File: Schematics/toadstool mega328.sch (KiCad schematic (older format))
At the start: 26 parts, among them CON1 BARREL_JACK, IC1 ATMEGA328P-P, K1 CAP_CONN_LHS, K2 CAP_CONN_RHS, K3 V-SELECT, K4 ICSP, K5 PIN 2-8, K6 PIN 21-28, K7 XTAL, K8 PIN 15-19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

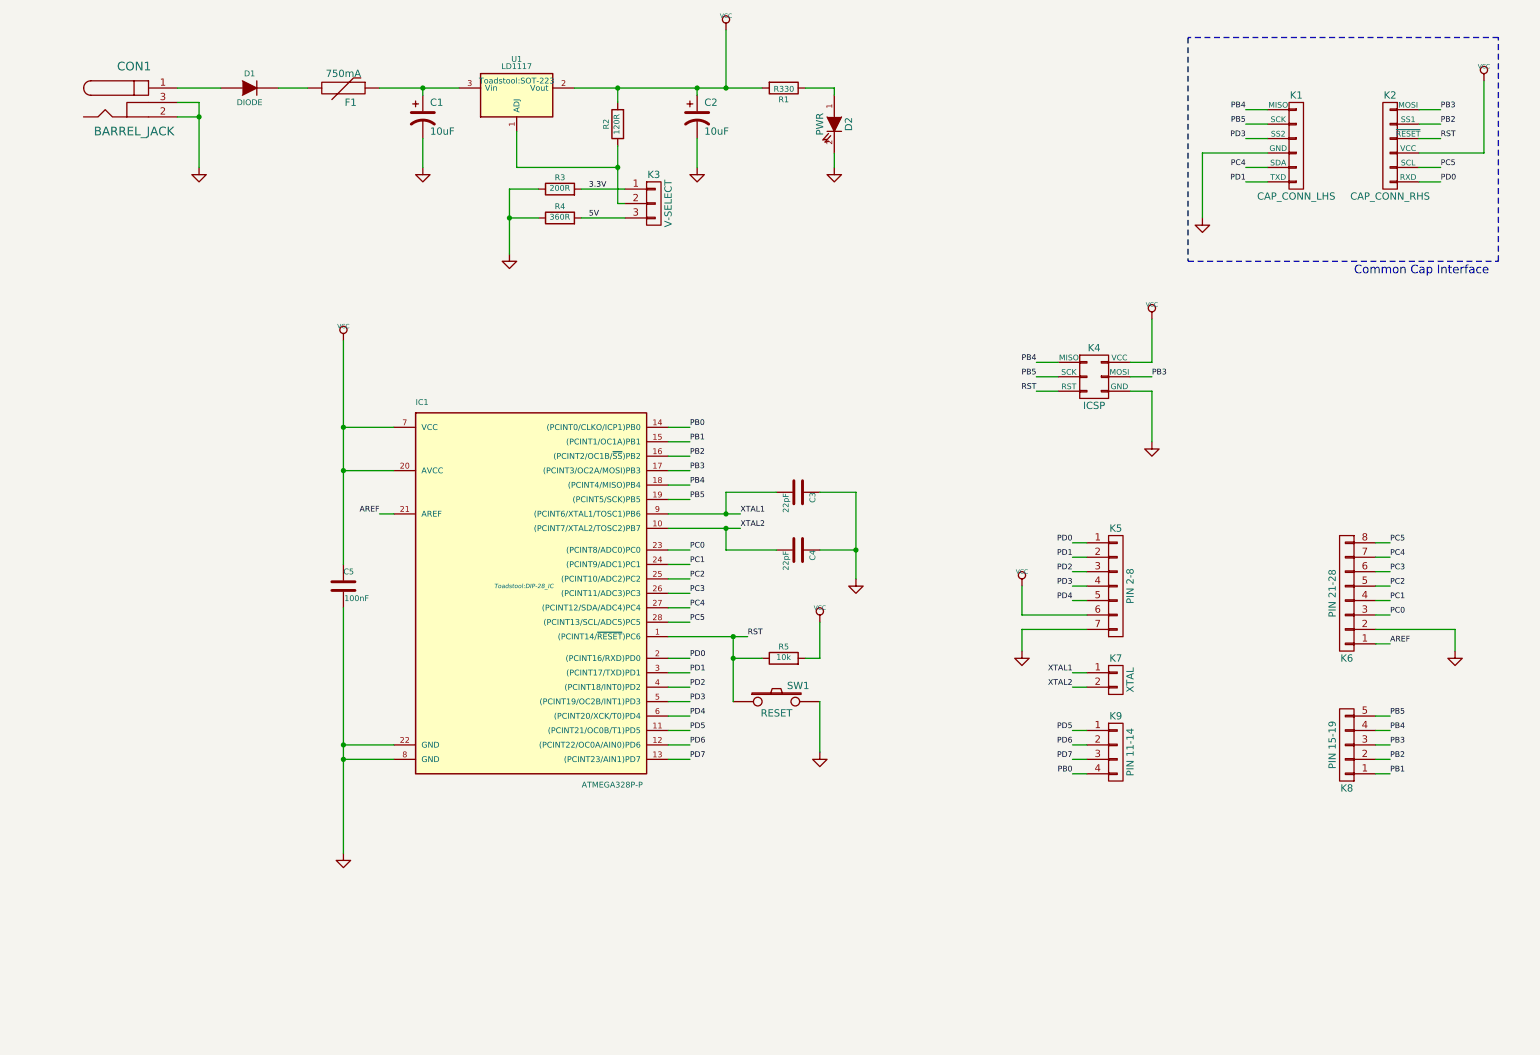
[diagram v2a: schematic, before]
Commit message: Cosmetic Changes to Silkscreen
Cosmetic Changes to Silkscreen
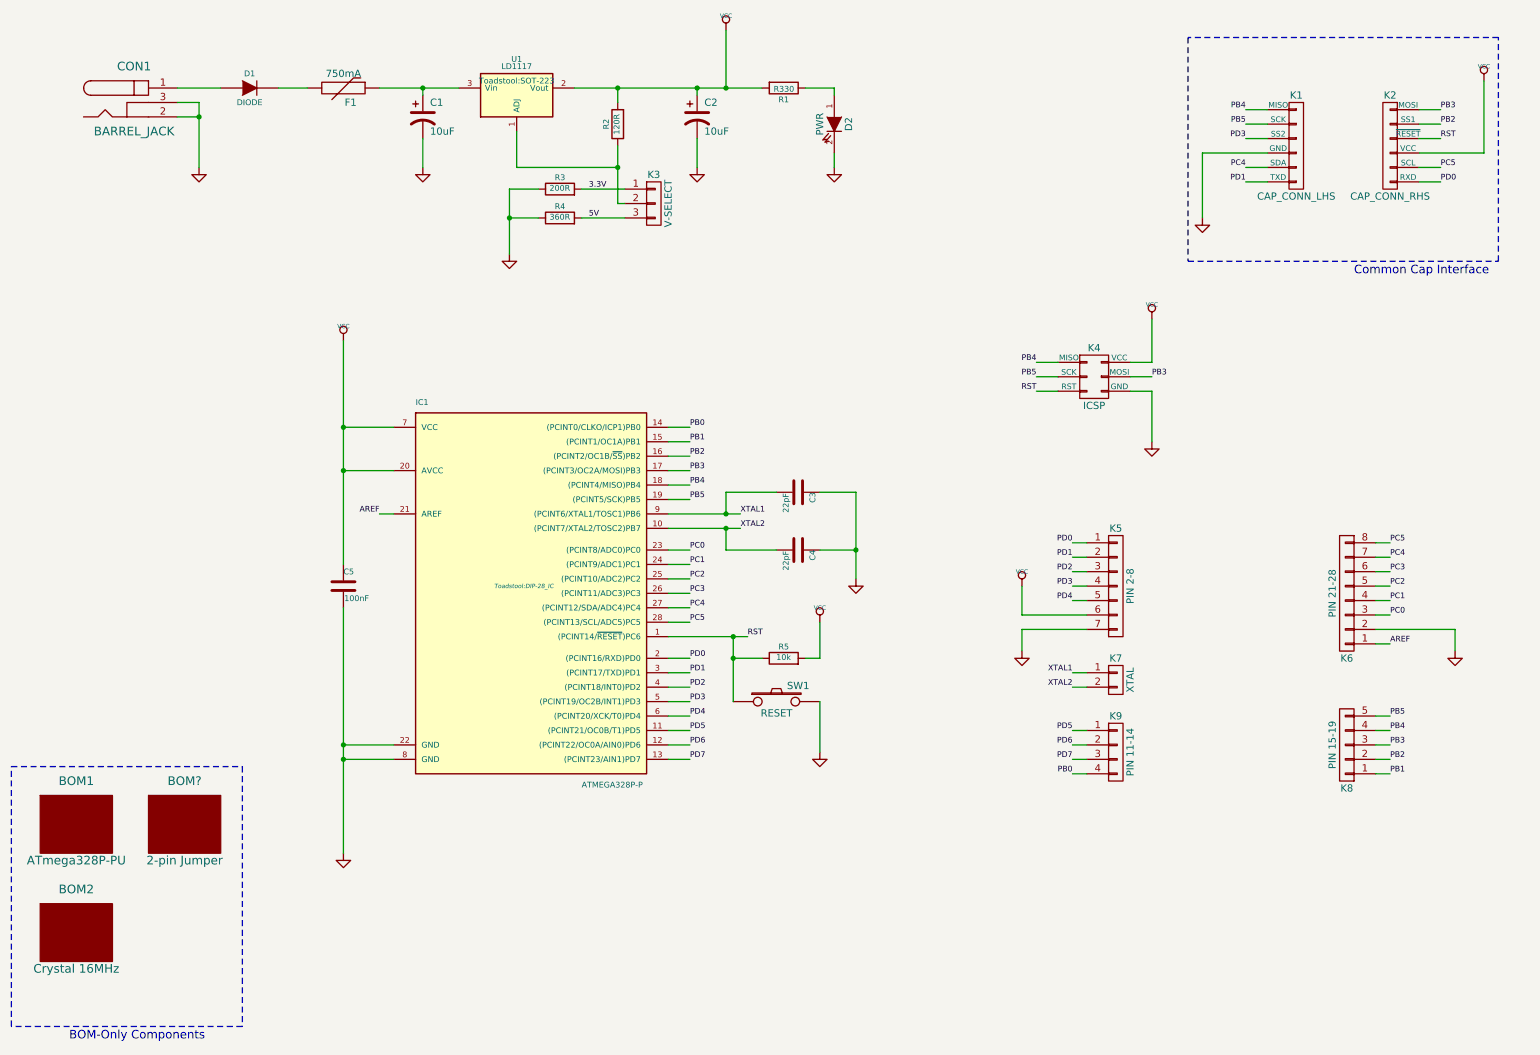
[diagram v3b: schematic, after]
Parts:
- added BOM1: ATmega328P-PU, symbol BOM
- added BOM2: Crystal 16MHz, symbol BOM
- added BOM?: 2-pin Jumper, symbol BOM
- C1, C2: Alt_Manufacturer (none) -> -; Alt_Mfg_Package_Suffix (none) -> -; Alt_Mfg_Part_No (none) -> -; Contract_Manuf_SKU (none) -> 302030059; Manufacturer (none) -> Nichicon; Mfg_Package_Suffix (none) -> -; Mfg_Part_No (none) -> UWX1C100MCL1GB
- C3, C4: Alt_Manufacturer (none) -> -; Alt_Mfg_Package_Suffix (none) -> -; Alt_Mfg_Part_No (none) -> -; Contract_Manuf_SKU (none) -> 0100620P1; Manufacturer (none) -> Kemet; Mfg_Package_Suffix (none) -> -; Mfg_Part_No (none) -> C0805C220J1GACTU
- C5: Alt_Manufacturer (none) -> -; Alt_Mfg_Package_Suffix (none) -> -; Alt_Mfg_Part_No (none) -> -; Contract_Manuf_SKU (none) -> 302010165; Manufacturer (none) -> Kemet; Mfg_Package_Suffix (none) -> -; Mfg_Part_No (none) -> C0805C104K5RACTU
- CON1: Alt_Manufacturer (none) -> Kobiconn; Alt_Mfg_Package_Suffix (none) -> -; Alt_Mfg_Part_No (none) -> 163-5010-E; Contract_Manuf_SKU (none) -> 3410020P1; Manufacturer (none) -> CUI Inc; Mfg_Package_Suffix (none) -> -; Mfg_Part_No (none) -> PJ-002A
- D1: Alt_Manufacturer (none) -> Diodes Inc; Alt_Mfg_Package_Suffix (none) -> -; Alt_Mfg_Part_No (none) -> 1N5817-T; Contract_Manuf_SKU (none) -> 0300070P1; Manufacturer (none) -> STMicroelectronics; Mfg_Package_Suffix (none) -> -; Mfg_Part_No (none) -> 1N5819
- D2: Alt_Manufacturer (none) -> Osram; Alt_Mfg_Package_Suffix (none) -> -; Alt_Mfg_Part_No (none) -> LH R974-LP-1; Contract_Manuf_SKU (none) -> 0330020P1; Manufacturer (none) -> Osram; Mfg_Package_Suffix (none) -> -; Mfg_Part_No (none) -> LH R974
- F1: Alt_Manufacturer (none) -> -; Alt_Mfg_Package_Suffix (none) -> -; Alt_Mfg_Part_No (none) -> -; Contract_Manuf_SKU (none) -> 307010010; Manufacturer (none) -> TE Connectivity; Mfg_Package_Suffix (none) -> -; Mfg_Part_No (none) -> MICROSMD050F-2
- IC1: Alt_Manufacturer (none) -> 3M; Alt_Mfg_Package_Suffix (none) -> -; Alt_Mfg_Part_No (none) -> 4828-3004-CP; Contract_Manuf_SKU (none) -> -; Manufacturer (none) -> Assmann; Mfg_Package_Suffix (none) -> -; Mfg_Part_No (none) -> A 28-LC/7-T
- K1, K2: Alt_Manufacturer (none) -> 4UConnector; Alt_Mfg_Package_Suffix (none) -> -; Alt_Mfg_Part_No (none) -> 15170; Contract_Manuf_SKU (none) -> -; Manufacturer (none) -> Samtec; Mfg_Package_Suffix (none) -> -; Mfg_Part_No (none) -> ESQ-106-12-G-S
- K3: Alt_Manufacturer (none) -> -; Alt_Mfg_Package_Suffix (none) -> -; Alt_Mfg_Part_No (none) -> -; Contract_Manuf_SKU (none) -> 3460810P1; Manufacturer (none) -> Harwin; Mfg_Package_Suffix (none) -> -; Mfg_Part_No (none) -> M20-9990345
- K4: Alt_Manufacturer (none) -> -; Alt_Mfg_Package_Suffix (none) -> -; Alt_Mfg_Part_No (none) -> -; Contract_Manuf_SKU (none) -> 3460180P1; Manufacturer (none) -> 3M; Mfg_Package_Suffix (none) -> -; Mfg_Part_No (none) -> 30306-6002HB
- K5: Alt_Manufacturer (none) -> -; Alt_Mfg_Package_Suffix (none) -> -; Alt_Mfg_Part_No (none) -> -; Contract_Manuf_SKU (none) -> -; Manufacturer (none) -> Wurth; Mfg_Package_Suffix (none) -> -; Mfg_Part_No (none) -> 61300711121
- K6: Alt_Manufacturer (none) -> -; Alt_Mfg_Package_Suffix (none) -> -; Alt_Mfg_Part_No (none) -> -; Contract_Manuf_SKU (none) -> 3461050P1; Manufacturer (none) -> Wurth; Mfg_Package_Suffix (none) -> -; Mfg_Part_No (none) -> 61300811121
- K7: Alt_Manufacturer (none) -> -; Alt_Mfg_Package_Suffix (none) -> -; Alt_Mfg_Part_No (none) -> -; Contract_Manuf_SKU (none) -> 320030023; Manufacturer (none) -> Preci-dip; Mfg_Package_Suffix (none) -> -; Mfg_Part_No (none) -> 310-87-102-41-001101
- K8: Alt_Manufacturer (none) -> -; Alt_Mfg_Package_Suffix (none) -> -; Alt_Mfg_Part_No (none) -> -; Contract_Manuf_SKU (none) -> -; Manufacturer (none) -> Wurth; Mfg_Package_Suffix (none) -> -; Mfg_Part_No (none) -> 61300511121
- K9: Alt_Manufacturer (none) -> -; Alt_Mfg_Package_Suffix (none) -> -; Alt_Mfg_Part_No (none) -> -; Contract_Manuf_SKU (none) -> 320020017; Manufacturer (none) -> Wurth; Mfg_Package_Suffix (none) -> -; Mfg_Part_No (none) -> 61300411121
- R1: Alt_Manufacturer (none) -> Samsung; Alt_Mfg_Package_Suffix (none) -> -; Alt_Mfg_Part_No (none) -> RC2012F331CS; Contract_Manuf_SKU (none) -> 0011330P1; Manufacturer (none) -> TE Connectivity; Mfg_Package_Suffix (none) -> -; Mfg_Part_No (none) -> CRG0805F330R
- R2: Alt_Manufacturer (none) -> Samsung; Alt_Mfg_Package_Suffix (none) -> -; Alt_Mfg_Part_No (none) -> RC2012F121CS; Contract_Manuf_SKU (none) -> 301010194; Manufacturer (none) -> Panasonic; Mfg_Package_Suffix (none) -> -; Mfg_Part_No (none) -> ERJ-6ENF1200V
- R3: Alt_Manufacturer (none) -> Samsung; Alt_Mfg_Package_Suffix (none) -> -; Alt_Mfg_Part_No (none) -> RC2012F201CS; Contract_Manuf_SKU (none) -> -; Manufacturer (none) -> Panasonic; Mfg_Package_Suffix (none) -> -; Mfg_Part_No (none) -> ERJ-6ENF2000V
- R4: Alt_Manufacturer (none) -> Yageo; Alt_Mfg_Package_Suffix (none) -> -; Alt_Mfg_Part_No (none) -> RC0805FR-07360RL; Contract_Manuf_SKU (none) -> -; Manufacturer (none) -> Panasonic; Mfg_Package_Suffix (none) -> -; Mfg_Part_No (none) -> ERJ-6ENF3600V
- R5: Alt_Manufacturer (none) -> Yageo; Alt_Mfg_Package_Suffix (none) -> -; Alt_Mfg_Part_No (none) -> RC0805JR-0710KL; Contract_Manuf_SKU (none) -> 0011240P1; Manufacturer (none) -> TE Connectivity; Mfg_Package_Suffix (none) -> -; Mfg_Part_No (none) -> CRG0805F10K
- SW1: Alt_Manufacturer (none) -> Alps; Alt_Mfg_Package_Suffix (none) -> -; Alt_Mfg_Part_No (none) -> SKQGAFE010; Contract_Manuf_SKU (none) -> 311020017; Manufacturer (none) -> C and K Components; Mfg_Package_Suffix (none) -> -; Mfg_Part_No (none) -> KSEM31G LFS
- U1: Alt_Manufacturer (none) -> -; Alt_Mfg_Package_Suffix (none) -> -; Alt_Mfg_Part_No (none) -> -; Manufacturer (none) -> STMicroelectronics; Mfg_Package_Suffix (none) -> -; Mfg_Part_No (none) -> LD1117STR
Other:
- note added: "BOM-Only Components"
